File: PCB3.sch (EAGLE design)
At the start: 48 parts

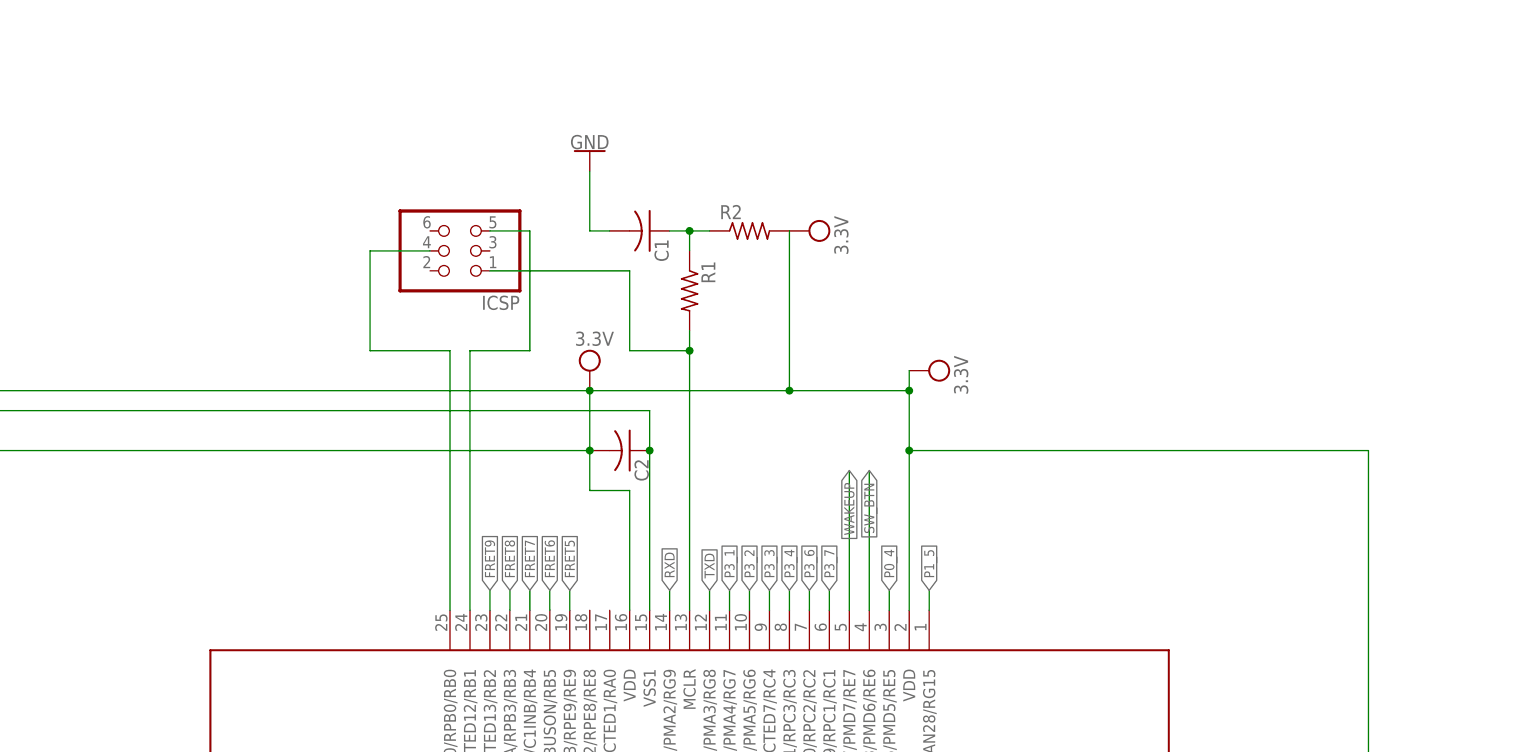
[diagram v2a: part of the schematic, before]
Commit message: Added pads for frets, redid traces from micro to other PCBs
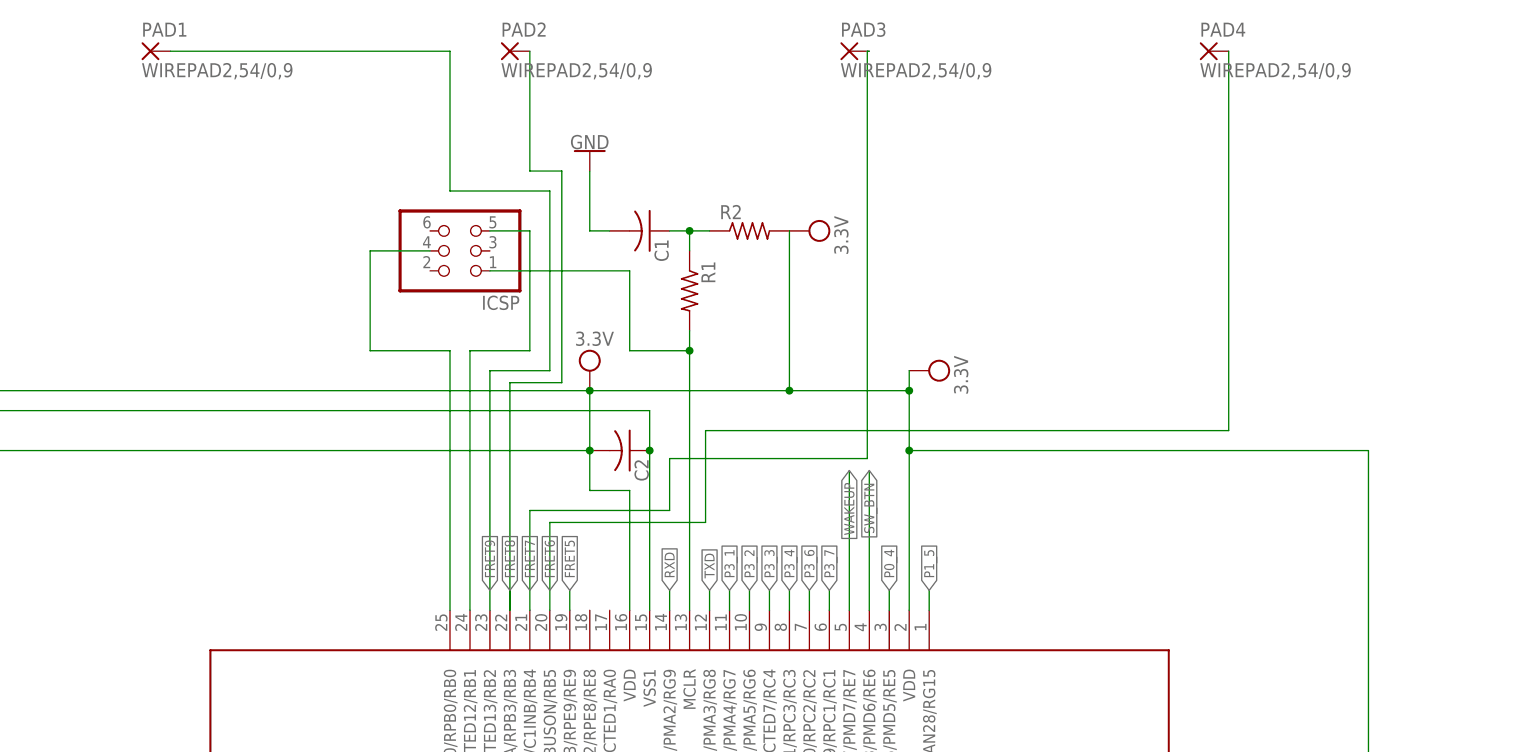
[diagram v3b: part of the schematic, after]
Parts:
- added PAD1, PAD2, PAD3, PAD4: WIREPAD2,54/0,9, wirepad:WIREPAD2,54/0,9
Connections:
- net FRET6: now also PAD4.P
- net FRET7: now also PAD3.P
- net FRET8: now also PAD2.P
- net FRET9: now also PAD1.P
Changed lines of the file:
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@@
 <part name="GND3" library="SparkFun-PowerSymbols" deviceset="GND" device=""/>
 <part name="GND4" library="SparkFun-PowerSymbols" deviceset="GND" device=""/>
+<part name="PAD1" library="wirepad" deviceset="WIREPAD" device="2,54/0,9"/>
+<part name="PAD2" library="wirepad" deviceset="WIREPAD" device="2,54/0,9"/>
+<part name="PAD3" library="wirepad" deviceset="WIREPAD" device="2,54/0,9"/>
+<part name="PAD4" library="wirepad" deviceset="WIREPAD" device="2,54/0,9"/>
 </parts>
 <sheets>
@@
 <instance part="GND3" gate="1" x="236.22" y="114.3"/>
 <instance part="GND4" gate="1" x="139.7" y="254" rot="R180"/>
+<instance part="PAD1" gate="G$1" x="83.82" y="266.7"/>
+<instance part="PAD2" gate="G$1" x="129.54" y="266.7"/>
+<instance part="PAD3" gate="G$1" x="172.72" y="266.7"/>
+<instance part="PAD4" gate="G$1" x="218.44" y="266.7"/>
 </instances>
 <busses>
@@
 <wire x1="129.54" y1="195.58" x2="129.54" y2="198.12" width="0.1524" layer="91"/>
 <label x="129.54" y="198.12" size="1.27" layer="95" rot="R90" xref="yes"/>
+<pinref part="PAD2" gate="G$1" pin="P"/>
+<wire x1="132.08" y1="266.7" x2="132.08" y2="251.46" width="0.1524" layer="91"/>
+<wire x1="132.08" y1="251.46" x2="136.144" y2="251.46" width="0.1524" layer="91"/>
+<wire x1="136.144" y1="251.46" x2="136.144" y2="224.536" width="0.1524" layer="91"/>
+<wire x1="136.144" y1="224.536" x2="129.54" y2="224.536" width="0.1524" layer="91"/>
+<wire x1="129.54" y1="224.536" x2="129.54" y2="195.58" width="0.1524" layer="91"/>
 </segment>
 </net>
@@
 <segment>
 <pinref part="U$2" gate="G$1" pin="PGEC3/AN2/CTCMP/C2INB/RPB2/CTED13/RB2"/>
-<wire x1="127" y1="195.58" x2="127" y2="198.12" width="0.1524" layer="91"/>
 <label x="127" y="198.12" size="1.27" layer="95" rot="R90" xref="yes"/>
+<pinref part="PAD1" gate="G$1" pin="P"/>
+<wire x1="86.36" y1="266.7" x2="121.92" y2="266.7" width="0.1524" layer="91"/>
+<wire x1="121.92" y1="266.7" x2="121.92" y2="248.92" width="0.1524" layer="91"/>
+<wire x1="121.92" y1="248.92" x2="134.62" y2="248.92" width="0.1524" layer="91"/>
+<wire x1="134.62" y1="248.92" x2="134.62" y2="226.06" width="0.1524" layer="91"/>
+<wire x1="134.62" y1="226.06" x2="127" y2="226.06" width="0.1524" layer="91"/>
+<wire x1="127" y1="226.06" x2="127" y2="195.58" width="0.1524" layer="91"/>
 </segment>
 </net>
@@
 <segment>
 <pinref part="U$2" gate="G$1" pin="AN4/C1INB/RB4"/>
-<wire x1="132.08" y1="195.58" x2="132.08" y2="198.12" width="0.1524" layer="91"/>
 <label x="132.08" y="198.12" size="1.27" layer="95" rot="R90" xref="yes"/>
+<pinref part="PAD3" gate="G$1" pin="P"/>
+<wire x1="175.26" y1="266.7" x2="175.006" y2="266.7" width="0.1524" layer="91"/>
+<wire x1="175.006" y1="266.7" x2="175.006" y2="214.884" width="0.1524" layer="91"/>
+<wire x1="175.006" y1="214.884" x2="149.86" y2="214.884" width="0.1524" layer="91"/>
+<wire x1="149.86" y1="214.884" x2="149.86" y2="208.28" width="0.1524" layer="91"/>
+<wire x1="149.86" y1="208.28" x2="132.08" y2="208.28" width="0.1524" layer="91"/>
+<wire x1="132.08" y1="208.28" x2="132.08" y2="195.58" width="0.1524" layer="91"/>
 </segment>
 </net>
@@
 <segment>
 <pinref part="U$2" gate="G$1" pin="AN5/C1INA/RPB5/VBUSON/RB5"/>
-<wire x1="134.62" y1="195.58" x2="134.62" y2="198.12" width="0.1524" layer="91"/>
 <label x="134.62" y="198.12" size="1.27" layer="95" rot="R90" xref="yes"/>
-</segment>
-</net>
+<pinref part="PAD4" gate="G$1" pin="P"/>
+<wire x1="220.98" y1="266.7" x2="220.98" y2="218.44" width="0.1524" layer="91"/>
+<wire x1="220.98" y1="218.44" x2="154.432" y2="218.44" width="0.1524" layer="91"/>
+<wire x1="154.432" y1="218.44" x2="154.432" y2="206.756" width="0.1524" layer="91"/>
+<wire x1="154.432" y1="206.756" x2="134.62" y2="206.756" width="0.1524" layer="91"/>
+<wire x1="134.62" y1="206.756" x2="134.62" y2="195.58" width="0.1524" layer="91"/>
+</segment>
+</net>

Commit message: Finished PCB1, PCB3, and added parts to ECE477 library
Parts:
- added C10: (no value), rcl:C-USC0805
- added C11: 10uF, rcl:C-USC0805
- added C12: 100uF, rcl:C-USC0805
- added D1: S1BFSCT, ECE477_Guitutar:S1BFSCT
- added H1, H2: MOUNT-HOLE2.8, holes:MOUNT-HOLE2.8
- added JP1, JP2: (no value), pinhead:PINHD-1X1
- added R10, R11, R12, R9: 330k, rcl:R-US_M0805
- added SJ1, SJ2, SJ3, SJ4: (no value), jumper:SJW
- added U$1, U$10, U$11, U$12, U$13, U$14, U$15, U$16, U$17, U$18, U$19, U$20, U$21, U$22, U$23, U$24, U$25, U$3, U$30, U$31, U$32, U$33, U$34, U$35, U$36, U$37, U$38, U$39, U$4, U$40, U$41, U$42, U$43, U$44, U$45, U$46, U$47, U$48, U$49, U$5, U$50, U$51, U$52, U$53, U$54, U$55, U$56, U$57, U$58, U$59, U$6, U$60, U$61, U$62, U$63, U$64, U$65, U$66, U$67, U$68, U$69, U$7, U$8, U$9: JUMPER, ECE477_Guitutar:JUMPER
- added U1: (no value), SparkFun-IC-Power:V_REG_LM1117SOT223
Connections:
- new net 5.2V_PB: C11.1, D1.P$1, JP1.1, U1.IN
- new net N$3: PAD1.P, R12.2
- new net N$4: PAD2.P, R11.2
- new net N$5: PAD3.P, R10.2
- new net N$7: PAD4.P, R9.2
- net FRET10: now also U$2.PGED3/AN3/C2INA/RPB3/RB3; no longer U$2.PGEC2/AN6/RPB6/RB6
- net FRET11: now also U$2.PGEC3/AN2/CTCMP/C2INB/RPB2/CTED13/RB2; no longer U$2.PGED2/AN7/RPB7/CTED3/RB7
- net FRET12: now also U$2.PGEC2/AN6/RPB6/RB6; no longer U$2.VREF-/PMA7/RA9
- net FRET13: now also U$2.PGED2/AN7/RPB7/CTED3/RB7; no longer U$2.VREF+/PMA6/RA10
- net FRET14: now also U$2.VREF-/PMA7/RA9; no longer U$2.AN8/RPB8/CTED10/RB8
- net FRET15: now also U$2.VREF+/PMA6/RA10; no longer U$2.AN9/RPB9/CTED4/RB9
- net FRET16: now also U$2.AN8/RPB8/CTED10/RB8; no longer U$2.CVREFOUT/AN10/RPB10/CTED11/PMA13/RB10
- net FRET17: now also U$2.AN9/RPB9/CTED4/RB9; no longer U$2.AN11/PMA12/RB11
- net FRET18: now also U$2.CVREFOUT/AN10/RPB10/CTED11/PMA13/RB10; no longer U$2.VSS2
- net FRET19: now also U$2.AN11/PMA12/RB11; no longer U$2.VDD@2
- net FRET5: now also U$2.TMS/CTED1/RA0; no longer U$2.AN33/RPE9/RE9
- net FRET6: now also R9.1, U$2.AN32/RPE8/RE8; no longer PAD4.P, U$2.AN5/C1INA/RPB5/VBUSON/RB5
- net FRET7: now also R10.1, U$2.AN33/RPE9/RE9; no longer PAD3.P, U$2.AN4/C1INB/RB4
- net FRET8: now also R11.1, U$2.AN5/C1INA/RPB5/VBUSON/RB5; no longer PAD2.P, U$2.PGED3/AN3/C2INA/RPB3/RB3
- net FRET9: now also R12.1, U$2.AN4/C1INB/RB4; no longer PAD1.P, U$2.PGEC3/AN2/CTCMP/C2INB/RPB2/CTED13/RB2
- net GND: now also C11.2, C12.2, JP2.1, SJ3.1, SJ3.2, SJ4.1, SJ4.2
- net VDD: now also C10.1, C12.1, D1.P$2, SJ1.1, SJ1.2, SJ2.1, SJ2.2, U$2.VDD@2, U1.OUT, U1.OUT@1
- net VSS: now also C10.2, U$2.VSS2
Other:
- note added: "PowerBoost 1000 Circuit"
- note added: "To PCBs 1 and 2"
- note added: "To PCBs 4 and 5"
- moved on the sheet: PAD3

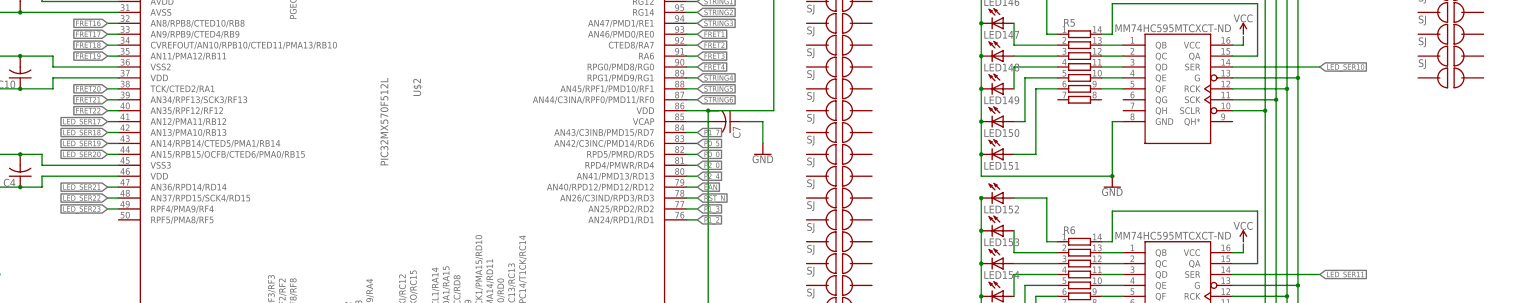
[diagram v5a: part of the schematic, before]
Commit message: Added pin AMP to micro for amplifier circuit
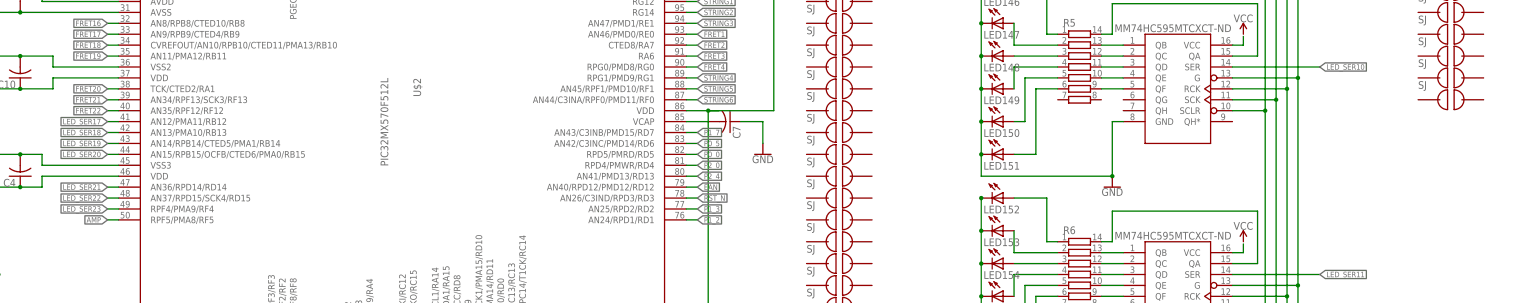
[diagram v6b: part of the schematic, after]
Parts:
- added U$70: JUMPER, ECE477_Guitutar:JUMPER
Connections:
- new net AMP: U$2.RPF5/PMA8/RF5
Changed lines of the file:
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@@
 <part name="R11" library="rcl" deviceset="R-US_" device="M0805" value="330k"/>
 <part name="R12" library="rcl" deviceset="R-US_" device="M0805" value="330k"/>
+<part name="U$70" library="ECE477_Guitutar" deviceset="JUMPER" device=""/>
 </parts>
 <sheets>
@@
 <instance part="R11" gate="G$1" x="132.08" y="259.08" rot="R90"/>
 <instance part="R12" gate="G$1" x="121.92" y="256.54" rot="R90"/>
+<instance part="U$70" gate="G$1" x="396.24" y="127"/>
 </instances>
 <busses>
@@
 </segment>
 </net>
+<net name="AMP" class="0">
+<segment>
+<pinref part="U$2" gate="G$1" pin="RPF5/PMA8/RF5"/>
+<wire x1="86.36" y1="99.06" x2="83.82" y2="99.06" width="0.1524" layer="91"/>
+<label x="83.82" y="99.06" size="1.27" layer="95" rot="R180" xref="yes"/>
+</segment>
+</net>

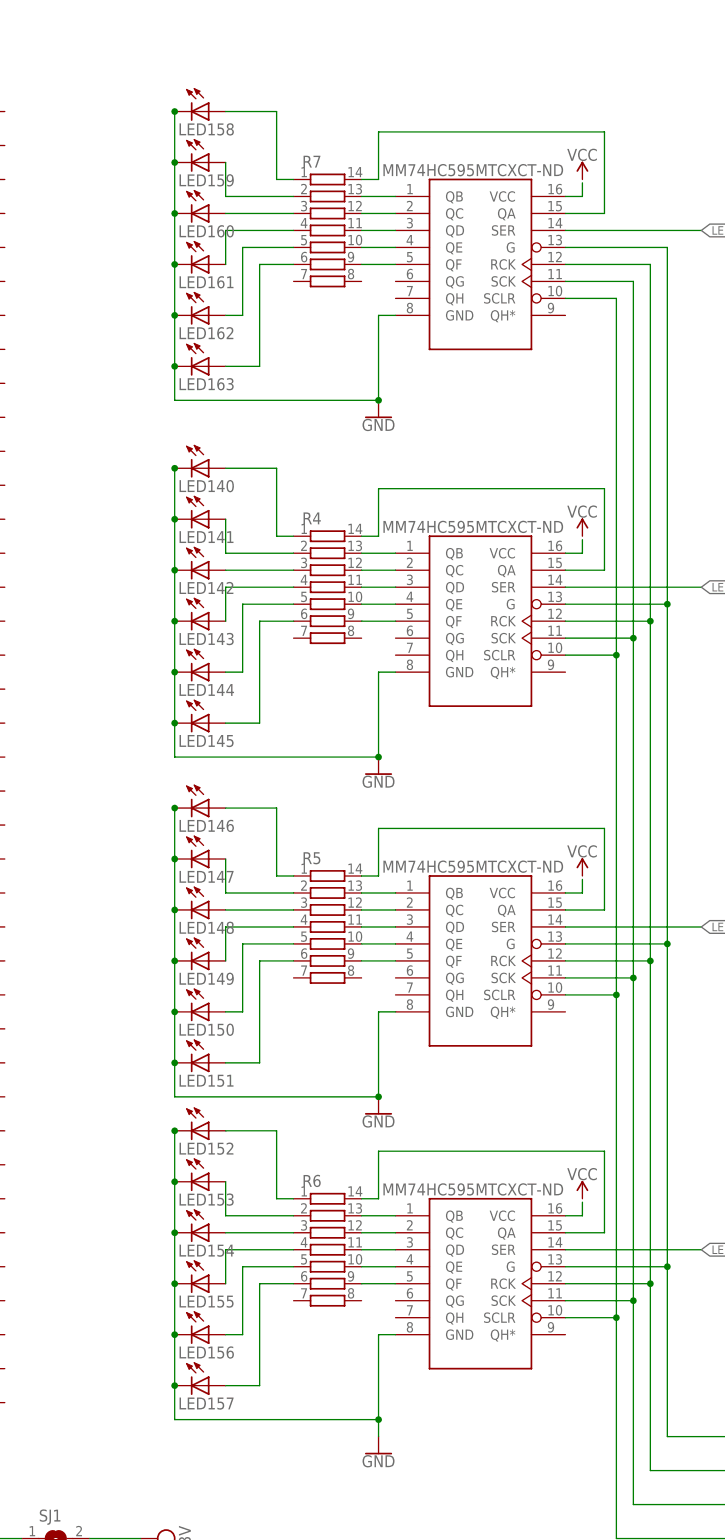
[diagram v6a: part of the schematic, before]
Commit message: Finished changing dimensions for PCB3 and switched out resistors for smaller ones.
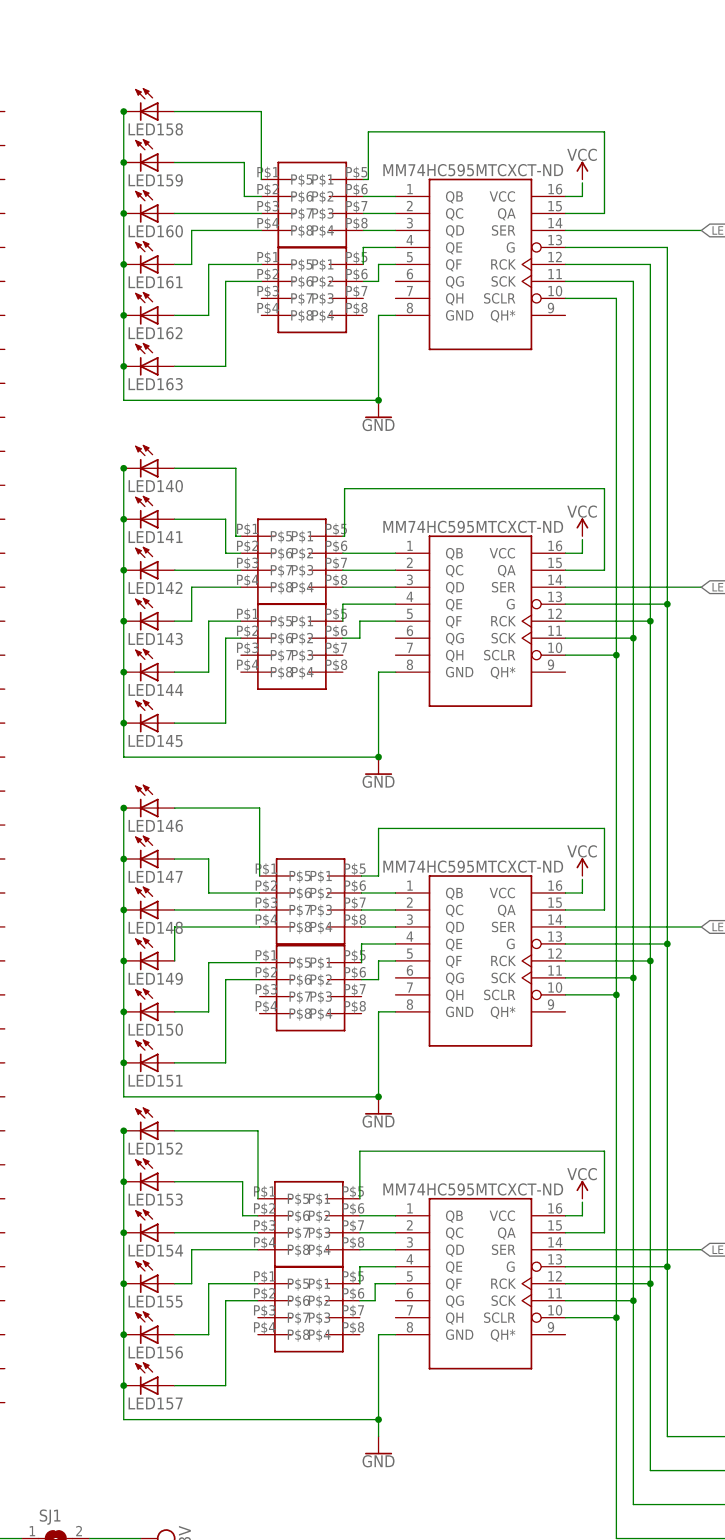
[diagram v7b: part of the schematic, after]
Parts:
- removed R4, R5, R6, R7: (no value), resistor-bourns:4814P-T01
- added U$71, U$72, U$73, U$74, U$75, U$76, U$77, U$78: MNR04MRAPJ680, ECE477_Guitutar:MNR04MRAPJ680
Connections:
- removed net N$102: LED153.A, R6.2
- removed net N$113: R7.13, U$26.QB
- removed net N$114: R7.12, U$26.QC
- removed net N$115: R7.11, U$26.QD
- removed net N$116: R7.10, U$26.QE
- removed net N$123: R7.9, U$26.QF
- removed net N$127: LED160.A, R7.3
- removed net N$75: R5.9, U$28.QF
- removed net N$78: LED146.A, R5.1
- removed net N$80: LED148.A, R5.3
- removed net N$81: LED149.A, R5.4
- removed net N$82: LED150.A, R5.5
- removed net N$83: LED151.A, R5.6
- removed net N$84: LED147.A, R5.2
- removed net N$90: R6.13, U$29.QB
- removed net N$91: R6.12, U$29.QC
- removed net N$92: R6.11, U$29.QD
- removed net N$93: R6.10, U$29.QE
- removed net N$94: R6.9, U$29.QF
- removed net N$98: LED154.A, R6.3
- removed net N$99: LED155.A, R6.4
- new net N$10: LED148.A, U$75.P$3
- new net N$15: LED149.A, U$75.P$4
- new net N$17: LED150.A, U$76.P$1
- new net N$18: LED151.A, U$76.P$2
- new net N$19: U$27.QB, U$73.P$6
- new net N$26: U$26.QB, U$71.P$6
- new net N$27: U$26.QC, U$71.P$7
- new net N$28: U$26.QD, U$71.P$8
- new net N$29: U$26.QE, U$72.P$5
- new net N$30: U$26.QF, U$72.P$6
- new net N$36: U$29.QB, U$77.P$6
- new net N$39: U$29.QC, U$77.P$7
- new net N$40: U$29.QD, U$77.P$8
- new net N$41: U$29.QE, U$78.P$5
- new net N$42: U$29.QF, U$78.P$6
- new net N$43: LED153.A, U$77.P$2
- new net N$44: LED154.A, U$77.P$3
- new net N$45: LED155.A, U$77.P$4
- new net N$6: U$28.QF, U$76.P$6
- new net N$8: LED146.A, U$75.P$1
- new net N$9: LED147.A, U$75.P$2
- net N$100: now also U$78.P$1; no longer R6.5
- net N$101: now also U$78.P$2; no longer R6.6
- net N$125: now also U$71.P$5; no longer R7.14
- net N$126: now also U$71.P$1; no longer R7.1
- net N$134: now also U$71.P$4; no longer R7.4
- net N$135: now also U$72.P$1; no longer R7.5
- net N$136: now also U$72.P$2; no longer R7.6
- net N$137: now also U$71.P$2; no longer R7.2
- net N$20: now also U$27.QC, U$73.P$7; no longer R4.13, U$27.QB
- net N$21: now also U$27.QD, U$73.P$8; no longer R4.12, U$27.QC
- net N$22: now also U$27.QE, U$74.P$5; no longer R4.11, U$27.QD
- net N$23: now also U$27.QF, U$74.P$6; no longer R4.10, U$27.QE
- net N$24: now also LED142.A, U$73.P$3; no longer R4.9, U$27.QF
- net N$31: now also U$73.P$5; no longer R4.14
- net N$32: now also U$73.P$1; no longer R4.1
- net N$33: now also U$73.P$2; no longer R4.2
- net N$34: now also LED160.A, U$71.P$3; no longer LED142.A, R4.3
- net N$35: now also U$73.P$4; no longer R4.4
- net N$46: now also U$74.P$1; no longer R4.5
- net N$47: now also U$74.P$2; no longer R4.6
- net N$62: now also U$75.P$6; no longer R5.13
- net N$63: now also U$75.P$7; no longer R5.12
- net N$64: now also U$75.P$8; no longer R5.11
- net N$74: now also U$76.P$5; no longer R5.10
- net N$77: now also U$75.P$5; no longer R5.14
- net N$96: now also U$77.P$5; no longer R6.14
- net N$97: now also U$77.P$1; no longer R6.1
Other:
- moved on the sheet: LED140, LED141, LED142, LED143, LED144, LED145, LED146, LED147, LED148, LED149, LED150, LED151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
